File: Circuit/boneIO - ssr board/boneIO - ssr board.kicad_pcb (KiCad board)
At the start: 2 copper layers, 169 x 102 mm, 45 parts, among them J1 Screw_Terminal_01x04, J10 Screw_Terminal_01x04, J11 Screw_Terminal_01x04, J2 Screw_Terminal_01x04, J3 Conn_02x13_Odd_Even, J4 Screw_Terminal_01x04, J5 Screw_Terminal_01x04, J6 Screw_Terminal_01x04, J7 Screw_Terminal_01x04, J8 Screw_Terminal_01x04, J9 Screw_Terminal_01x04, K21 HF46F, U1 MCP9808_MSOP, U2 ULN2803A, U3 ULN2803A, U4 ULN2803A

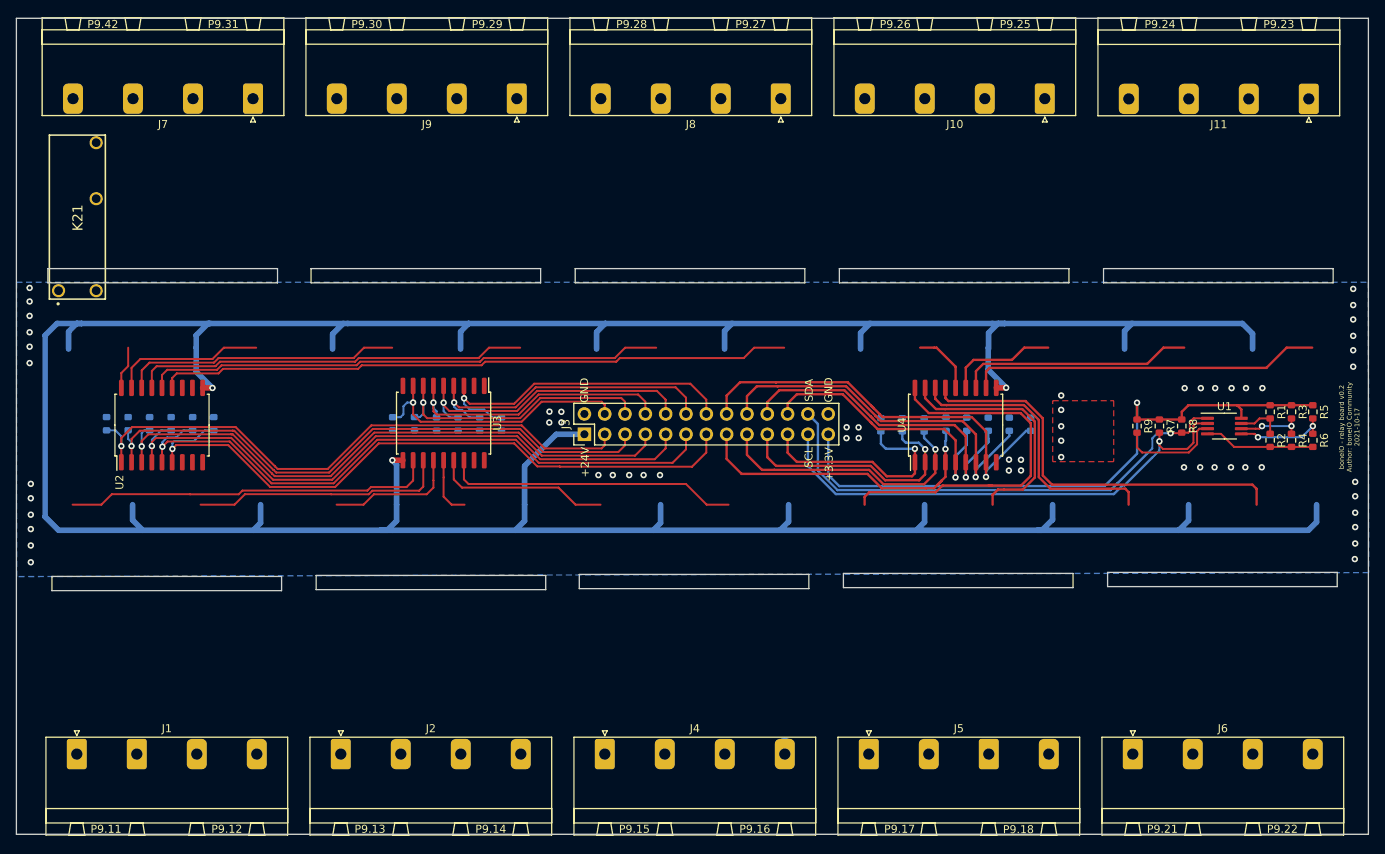
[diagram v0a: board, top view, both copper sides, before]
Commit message: Finished
Niestety przekombinowaliśmy z tymi ssr'ami i wyszła nam płytka ze zwykłymi przekaźnikami 5A - 30 sztuk. Niestety ssr'y nie zmieściły się na wysokość. Płytka w całości obsługiwana po i2c do zastosowania w module rozszerzeń lub w boneIO bezpośrednio.
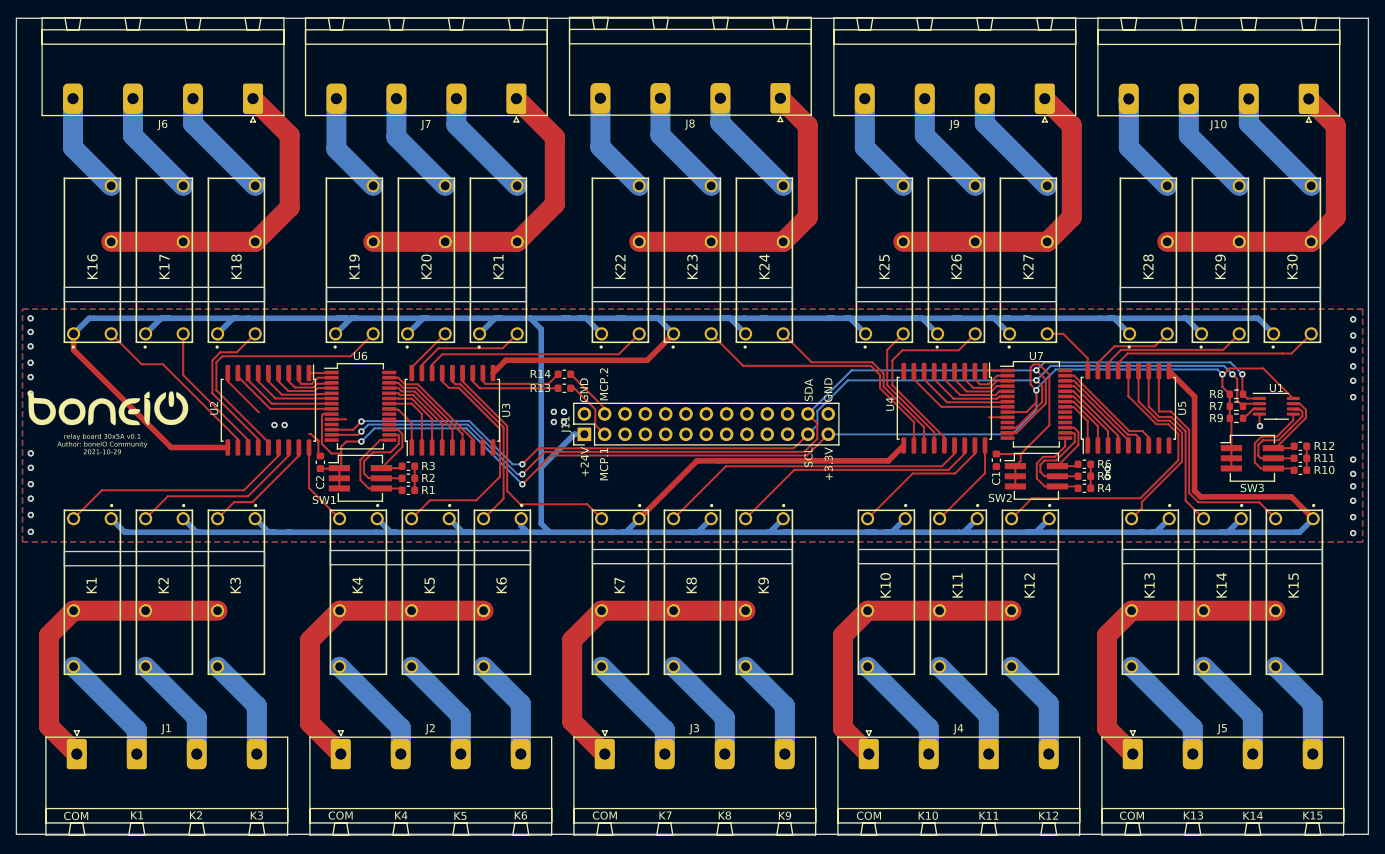
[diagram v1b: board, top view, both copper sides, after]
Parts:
- removed R15, R16, R17, R18, R19, R20, R21, R22, R23, R24, R25, R26, R27, R28, R29: 10k, Resistor_SMD:R_0603_1608Metric
- added C1: 100nF, Capacitor_SMD:C_0603_1608Metric, F.Cu at (410.6, 319.0)
- added C2: 100nF, Capacitor_SMD:C_0603_1608Metric, F.Cu at (326.1, 319.2)
- added G***: LOGO, boneIO_LOGO:boneIO_LOGO, F.Cu at (299.6, 312.5)
- added K1: HF46F, HF46F:HF46F, F.Cu at (297.6, 325.2)
- added K10: HF46F, HF46F:HF46F, F.Cu at (396.9, 325.2)
- added K11: HF46F, HF46F:HF46F, F.Cu at (405.9, 325.2)
- added K12: HF46F, HF46F:HF46F, F.Cu at (414.9, 325.2)
- added K13: HF46F, HF46F:HF46F, F.Cu at (429.9, 325.2)
- added K14: HF46F, HF46F:HF46F, F.Cu at (438.9, 325.2)
- added K15: HF46F, HF46F:HF46F, F.Cu at (447.9, 325.2)
- added K16: HF46F, HF46F:HF46F, F.Cu at (297.6, 304.2)
- added K17: HF46F, HF46F:HF46F, F.Cu at (306.6, 304.2)
- added K18: HF46F, HF46F:HF46F, F.Cu at (315.6, 304.2)
- added K19: HF46F, HF46F:HF46F, F.Cu at (330.4, 304.2)
- added K2: HF46F, HF46F:HF46F, F.Cu at (306.6, 325.2)
- added K20: HF46F, HF46F:HF46F, F.Cu at (339.4, 304.2)
- added K22: HF46F, HF46F:HF46F, F.Cu at (363.6, 304.2)
- added K23: HF46F, HF46F:HF46F, F.Cu at (372.6, 304.2)
- added K24: HF46F, HF46F:HF46F, F.Cu at (381.6, 304.2)
- added K25: HF46F, HF46F:HF46F, F.Cu at (396.6, 304.2)
- added K26: HF46F, HF46F:HF46F, F.Cu at (405.6, 304.2)
- added K27: HF46F, HF46F:HF46F, F.Cu at (414.6, 304.2)
- added K28: HF46F, HF46F:HF46F, F.Cu at (429.6, 304.2)
- added K29: HF46F, HF46F:HF46F, F.Cu at (438.6, 304.2)
- added K3: HF46F, HF46F:HF46F, F.Cu at (315.6, 325.2)
- added K30: HF46F, HF46F:HF46F, F.Cu at (447.6, 304.2)
- added K4: HF46F, HF46F:HF46F, F.Cu at (330.9, 325.2)
- added K5: HF46F, HF46F:HF46F, F.Cu at (339.9, 325.2)
- added K6: HF46F, HF46F:HF46F, F.Cu at (348.9, 325.2)
- added K7: HF46F, HF46F:HF46F, F.Cu at (363.6, 325.2)
- added K8: HF46F, HF46F:HF46F, F.Cu at (372.6, 325.2)
- added K9: HF46F, HF46F:HF46F, F.Cu at (381.6, 325.2)
- added SW1: SW_DIP_x03, Button_Switch_SMD:SW_DIP_SPSTx03_Slide_KingTek_DSHP03TJ_W5.25mm_P1.27mm_JPin, F.Cu at (331.1, 321.2)
- added SW2: SW_DIP_x03, Button_Switch_SMD:SW_DIP_SPSTx03_Slide_KingTek_DSHP03TJ_W5.25mm_P1.27mm_JPin, F.Cu at (415.6, 321.0)
- added SW3: SW_DIP_x03, Button_Switch_SMD:SW_DIP_SPSTx03_Slide_KingTek_DSHP03TJ_W5.25mm_P1.27mm_JPin, F.Cu at (442.6, 318.7)
- added U5: ULN2803A, Package_SO:SOIC-18W_7.5x11.6mm_P1.27mm, F.Cu at (427.1, 312.5)
- added U6: MCP23017_SS, Package_SO:SSOP-28_5.3x10.2mm_P0.65mm, F.Cu at (331.1, 312.2)
- added U7: MCP23017_SS, Package_SO:SSOP-28_5.3x10.2mm_P0.65mm, F.Cu at (415.6, 312.0)
- K21: footprint HF46F -> HF46F:HF46F
- R1, R2, R3, R4, R5, R6: value 0k -> 10k
- R10, R11, R12: moved to F.Cu
- R13, R14: value 10k -> 0; moved to F.Cu
- moved R12 141.2 mm to (448.6, 317.2), turned to 0 degrees
- moved R11 138.5 mm to (448.6, 318.7), turned to 0 degrees
- moved R10 136.0 mm to (448.6, 320.2), turned to 0 degrees
- moved R3 110.6 mm to (337.1, 319.7), turned to 0 degrees
- moved R1 108.2 mm to (337.1, 322.7), turned to 0 degrees
- moved R2 107.8 mm to (337.1, 321.2), turned to 0 degrees
- moved R14 54.9 mm to (356.6, 308.2), turned to 0 degrees
- moved K21 52.9 mm to (348.4, 304.2)
- moved R13 52.0 mm to (356.6, 310.0), turned to 180 degrees
- moved J7 33.1 mm to (350.6, 273.8)
- moved J8 33.0 mm to (383.6, 273.7)
- moved R5 29.7 mm to (421.6, 321.0), turned to 0 degrees
- moved R6 28.7 mm to (421.6, 319.5), turned to 0 degrees
- moved R4 26.6 mm to (421.6, 322.5), turned to 0 degrees
- moved U2 13.4 mm to (319.6, 312.7), turned to 270 degrees
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- renumbered J11 to J10, J3 to J11, J4 to J3, J5 to J4, J6 to J5, J7 to J6, J8 to J7, J9 to J8, J10 to J9
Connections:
- J11 pad 3: Net-(J3-Pad3) (its old number) -> MCP.1
- J11 pad 4: Net-(J3-Pad4) (its old number) -> MCP.2
- J7 pad 1: Net-(J8-Pad1) (its old number) -> Net-(J7-Pad1)
- J7 pad 2: Net-(J8-Pad2) (its old number) -> Net-(J7-Pad2)
- K21 pad 1: Net-(K21-Pad1) -> +24V
- K21 pad 2: Net-(K21-Pad2) -> RELAY21
- K21 pad 3: Net-(K21-Pad3) -> Net-(J7-Pad1)
- K21 pad 4: Net-(K21-Pad4) -> Net-(J7-Pad2)
- R1 pad 1: +3V3 -> Net-(R1-Pad1)
- R1 pad 2: Net-(R1-Pad2) -> GND
- R10 pad 1: K8 -> Net-(R10-Pad1)
- R11 pad 1: K7 -> Net-(R11-Pad1)
- R12 pad 1: K15 -> Net-(R12-Pad1)
- R13 pad 1: K6 -> MCP.1
- R13 pad 2: GND -> Net-(R13-Pad2)
- R14 pad 1: K14 -> Net-(R14-Pad1)
- R14 pad 2: GND -> MCP.2
- R2 pad 1: Net-(R1-Pad2) -> Net-(R2-Pad1)
- R3 pad 1: +3V3 -> Net-(R3-Pad1)
- R3 pad 2: Net-(R3-Pad2) -> GND
- R4 pad 1: Net-(R3-Pad2) -> Net-(R4-Pad1)
- R5 pad 1: +3V3 -> Net-(R5-Pad1)
- R5 pad 2: Net-(R5-Pad2) -> GND
- R6 pad 1: Net-(R5-Pad2) -> Net-(R6-Pad1)
- U1 pad 5: Net-(R5-Pad2) -> Net-(R10-Pad1)
- U1 pad 6: Net-(R3-Pad2) -> Net-(R11-Pad1)
- U1 pad 7: Net-(R1-Pad2) -> Net-(R12-Pad1)
- U2 pad 1: K1 -> Net-(U2-Pad1)
- U2 pad 11: RELAY8 -> RELAY16
- U2 pad 12: RELAY7 -> RELAY17
- U2 pad 13: RELAY6 -> RELAY18
- U2 pad 14: RELAY5 -> RELAY19
- U2 pad 15: RELAY4 -> RELAY1
- U2 pad 16: RELAY3 -> RELAY2
- U2 pad 17: RELAY2 -> RELAY3
- U2 pad 18: RELAY1 -> RELAY4
- U2 pad 2: K2 -> Net-(U2-Pad2)
- U2 pad 3: K3 -> Net-(U2-Pad3)
- U2 pad 4: K4 -> Net-(U2-Pad4)
- U2 pad 5: K5 -> Net-(U2-Pad5)
- U2 pad 6: K6 -> Net-(U2-Pad6)
- U2 pad 7: K7 -> Net-(U2-Pad7)
- U2 pad 8: K8 -> Net-(U2-Pad8)
- U3 pad 1: K9 -> Net-(U3-Pad1)
- U3 pad 11: Net-(U3-Pad11) -> Net-(R14-Pad1)
- U3 pad 12: RELAY15 -> Net-(R13-Pad2)
- U3 pad 13: RELAY14 -> RELAY7
- U3 pad 14: RELAY13 -> RELAY6
- U3 pad 15: RELAY12 -> RELAY5
- U3 pad 16: RELAY11 -> RELAY22
- U3 pad 17: RELAY10 -> RELAY21
- U3 pad 18: RELAY9 -> RELAY20
- U3 pad 2: K10 -> Net-(U3-Pad2)
- U3 pad 3: K11 -> Net-(U3-Pad3)
- U3 pad 4: K12 -> Net-(U3-Pad4)
- U3 pad 5: K13 -> Net-(U3-Pad5)
- U3 pad 6: K14 -> Net-(U3-Pad6)
- U3 pad 7: K15 -> Net-(U3-Pad7)
- U4 pad 1: K16 -> Net-(U4-Pad1)
- U4 pad 12: RELAY22 -> RELAY24
- U4 pad 13: RELAY21 -> RELAY25
- U4 pad 14: RELAY20 -> RELAY26
- U4 pad 15: RELAY19 -> RELAY8
- U4 pad 16: RELAY18 -> RELAY9
- U4 pad 17: RELAY17 -> RELAY10
- U4 pad 18: RELAY16 -> RELAY11
- U4 pad 2: K17 -> Net-(U4-Pad2)
- U4 pad 3: K18 -> Net-(U4-Pad3)
- U4 pad 4: K19 -> Net-(U4-Pad4)
- U4 pad 5: K20 -> Net-(U4-Pad5)
- U4 pad 6: K21 -> Net-(U4-Pad6)
- U4 pad 7: K22 -> Net-(U4-Pad7)
- U4 pad 8: K23 -> Net-(U4-Pad8)
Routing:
- net +3V3: track 79.6 -> 191.6 mm, vias 1 -> 4
- net +24V: track 443.2 -> 555.0 mm, vias 3 -> 0
- net K6: track 83.8 -> 0.00 mm, vias 1 -> 0
- net K5: track 80.9 -> 0.00 mm, vias 1 -> 0
- net SDA: track 62.6 -> 142.6 mm, vias 1 -> 4
- net K4: track 78.6 -> 0.00 mm, vias 1 -> 0
- net K3: track 76.3 -> 0.00 mm, vias 1 -> 0
- net K1: track 74.6 -> 0.00 mm, vias 1 -> 0
- net K2: track 74.5 -> 0.00 mm, vias 1 -> 0
- net SCL: track 63.5 -> 137.3 mm, vias 1 -> 4
- net RELAY6: track 79.3 -> 22.3 mm
- net K17: track 52.5 -> 0.00 mm, vias 1 -> 0
- net K18: track 47.0 -> 0.00 mm, vias 1 -> 0
- net Net-(U3-Pad11): track 46.4 -> 0.00 mm
- net K19: track 42.3 -> 0.00 mm, vias 1 -> 0
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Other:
- outline, holes or cut-outs redrawn
- board text added: "COM"
- board text added: "K1"
- board text added: "K10"
- board text added: "K11"
- board text added: "K12"
- board text added: "K13"
- board text added: "K14"
- board text added: "K15"
- board text added: "K2"
- board text added: "K3"
- board text added: "K4"
- board text added: "K5"
- board text added: "K6"
- board text added: "K7"
- board text added: "K8"
- board text added: "K9"
- board text added: "MCP.1"
- board text added: "MCP.2"
- board text added: "relay board 30x5A v0.1 Author: boneIO Community 2021-10-29"
- board text removed: "P9.11"
- board text removed: "P9.12"
- board text removed: "P9.13"
- board text removed: "P9.14"
- board text removed: "P9.15"
- board text removed: "P9.16"
- board text removed: "P9.17"
- board text removed: "P9.18"
- board text removed: "P9.21"
- board text removed: "P9.22"
- board text removed: "P9.23"
- board text removed: "P9.24"
- board text removed: "P9.25"
- board text removed: "P9.26"
- board text removed: "P9.27"
- board text removed: "P9.28"
- board text removed: "P9.29"
- board text removed: "P9.30"
- board text removed: "P9.31"
- board text removed: "P9.42"
- board text removed: "boneIO - relay board v0.2 Author: boneIO Community 2021-10-17"
